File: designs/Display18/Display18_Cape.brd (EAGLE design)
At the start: 71.8 x 58.4 mm, 28 parts, among them T1 3904, X5 SPI-LCD-(1.8IN)

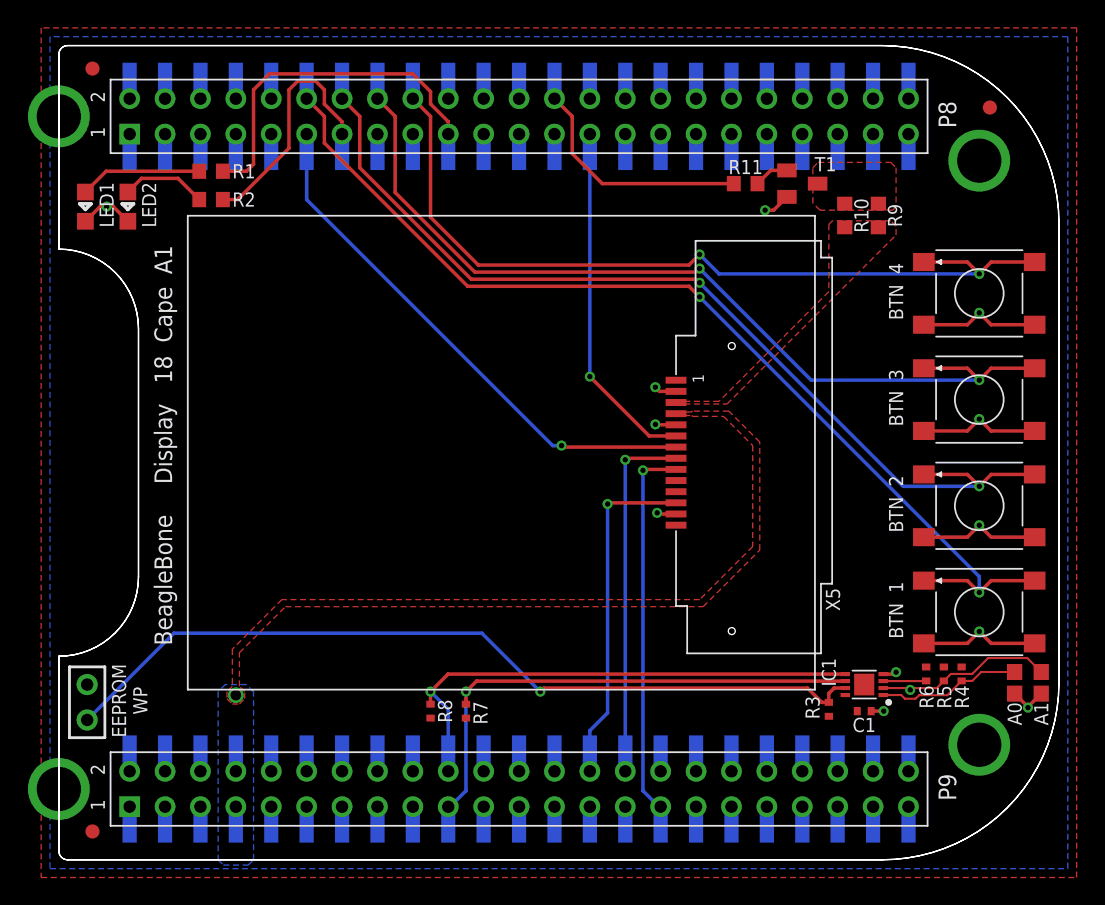
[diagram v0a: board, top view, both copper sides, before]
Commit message: Added the revised EAGLE schematics. Also removed two files that were probably not intended to be added as they are lock files in EAGLE.
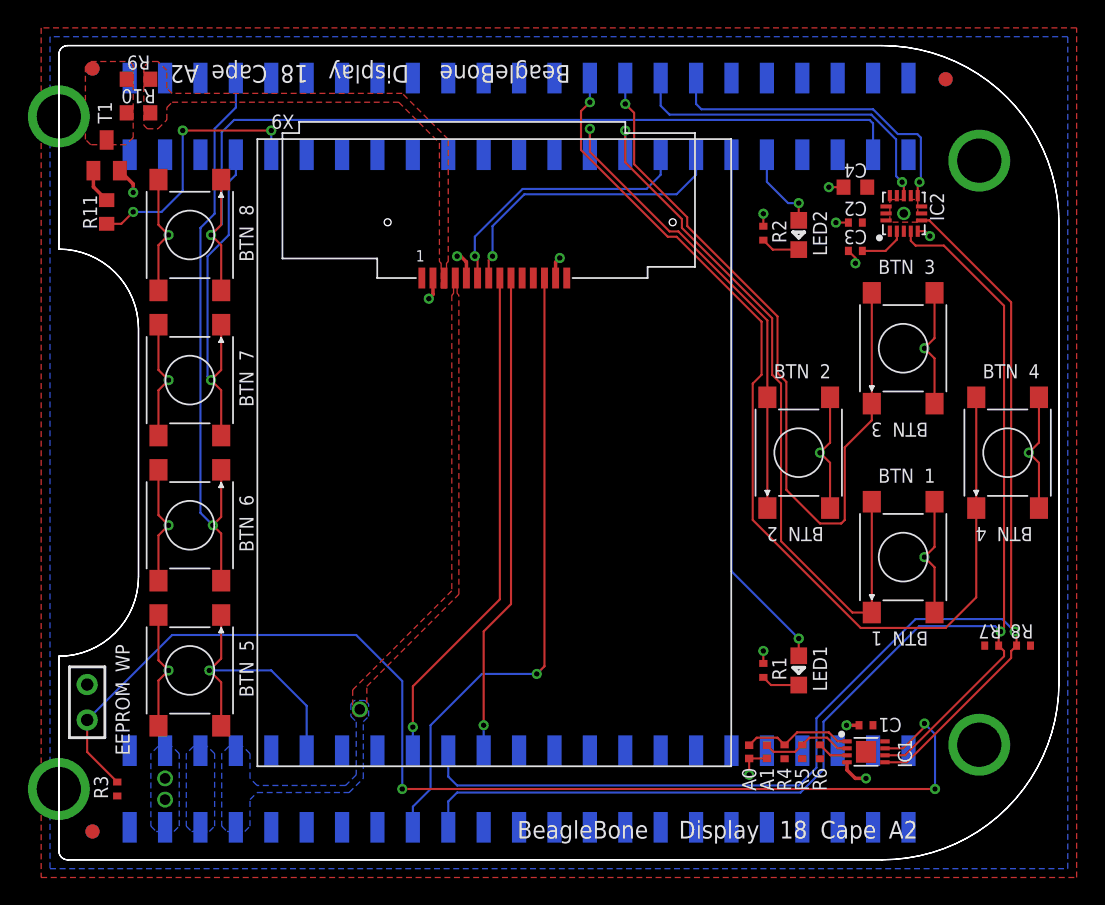
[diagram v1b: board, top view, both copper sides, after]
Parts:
- removed BB.CAPE1: BEAGLEBONE.CAPE.BOTTOM-ONLY-PADS.W/TH, GHI-Solutions:BEAGLEBONE.CAPE.BOTTOM-ONLY-PADS.W/TH
- added BB.CAPE2: BEAGLEBONE.CAPE.BOTTOM-ONLY-PADS, GHI-Solutions:BEAGLEBONE.CAPE.BOTTOM-ONLY-PADS
- added C2, C3: .1uF, GHI-BasicComponents:0402
- added C4: 4.7uF, GHI-BasicComponents:0603
- added FUD4, FUD5, FUD6: FIDUCIAL, GHI:FIDUCIAL_40MIL
- added IC2: (no value), GHI-IC:QFN-16-(MMA8453Q)
- added X6, X7, X8: (no value), GHI2:6MM_TACTILE-SWITCH
- added X9: SPI-LCD-(1.8IN), GHI-Connectors:LCD-(1.8IN)
- C1: value (none) -> .1uF
- R1, R2: device GHI-BasicComponents:0603 -> GHI-BasicComponents:0402
- SJ1, SJ2: device GHI-Miscellaneous:SOLDER.JOINT(0603) -> GHI-Miscellaneous:SOLDER.JOINT(0402)
- X5: value SPI-LCD-(1.8IN) -> (none); device GHI-Connectors:LCD-(1.8IN) -> GHI2:6MM_TACTILE-SWITCH
- moved LED1 61.0 mm to (53.1, 13.6)
- moved R9 54.0 mm to (5.71, 56.0), turned to 180 degrees
- moved R1 53.4 mm to (50.5, 13.6), turned to 270 degrees
- moved R3 51.4 mm to (4.19, 5.08)
- moved R10 51.2 mm to (5.71, 53.6), turned to 180 degrees
- moved T1 50.0 mm to (3.43, 50.5), turned to 0 degrees
- moved LED2 48.2 mm to (53.1, 44.8)
- moved R11 45.9 mm to (3.43, 46.5), turned to 270 degrees
- moved R8 42.8 mm to (69.2, 15.4), turned to 0 degrees
- moved R2 39.7 mm to (50.5, 45.0), turned to 270 degrees
- moved R7 38.0 mm to (66.9, 15.4), turned to 180 degrees
- moved X5 27.3 mm to (9.40, 13.6), turned to 270 degrees
- moved SJ2 20.3 mm to (50.8, 7.75)
- moved SJ1 19.7 mm to (49.5, 7.75)
- moved R4 13.9 mm to (52.1, 7.75), turned to 90 degrees
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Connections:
- removed net BTN1: BB.CAPE1.B8.12, BB.CAPE1.P8.12, X1.1, X1.2
- removed net BTN2: BB.CAPE1.B8.14, BB.CAPE1.P8.14, X2.1, X2.2
- removed net BTN3: BB.CAPE1.B8.16, BB.CAPE1.P8.16, X3.1, X3.2
- removed net BTN4: BB.CAPE1.B8.18, BB.CAPE1.P8.18, X4.1, X4.2
- removed net LCD.BACKLIGHT: BB.CAPE1.B8.26, BB.CAPE1.P8.26, R11.2
- removed net LCD.DC(GPIO45): BB.CAPE1.B8.11, BB.CAPE1.P8.11, X5.7
- removed net LCD.RESET(GPIO86): BB.CAPE1.B8.27, BB.CAPE1.P8.27, X5.6
- removed net LCD.SPI1.CS: BB.CAPE1.B9.28, BB.CAPE1.P9.28, X5.12
- removed net LCD.SPI1.MOSI: BB.CAPE1.B9.30, BB.CAPE1.P9.30, X5.8
- removed net LCD.SPI1.SCK: BB.CAPE1.B9.31, BB.CAPE1.P9.31, X5.9
- removed net LED1: BB.CAPE1.B8.19, BB.CAPE1.P8.19, R1.2
- removed net LED2: BB.CAPE1.B8.13, BB.CAPE1.P8.13, R2.2
- removed net N$282: LED1.A, R1.1
- removed net N$284: LED2.A, R2.1
- new net ACC.IRQ1(GPIO11): BB.CAPE2.B8.32, IC2.11
- new net ACC.IRQ2(GPIO81): BB.CAPE2.B8.34, IC2.9
- new net BTN.1(GPIO87): BB.CAPE2.B8.29, X1.1, X1.2
- new net BTN.2(GPIO86): BB.CAPE2.B8.27, X2.1, X2.2
- new net BTN.3(GPIO89): BB.CAPE2.B8.30, X3.1, X3.2
- new net BTN.4(GPIO88): BB.CAPE2.B8.28, X4.1, X4.2
- new net BTN.5(GPIO60): BB.CAPE2.B9.12, X5.1, X5.2
- new net BTN.6(GPIO67): BB.CAPE2.B8.8, X6.1, X6.2
- new net BTN.7(GPIO66): BB.CAPE2.B8.7, X7.1, X7.2
- new net BTN.8(GPIO72): BB.CAPE2.B8.43, X8.1, X8.2
- new net LCD.BACKLIGHT(TIMER5): BB.CAPE2.B8.9, R11.2
- new net LCD.DC(GPIO9): BB.CAPE2.B8.33, X9.7
- new net LCD.RESET(GPIO10): BB.CAPE2.B8.31, X9.6
- new net LCD.SPI0.CLK: BB.CAPE2.B9.22, X9.9
- new net LCD.SPI0.CS: BB.CAPE2.B9.17, X9.12
- new net LCD.SPI0.MOSI: BB.CAPE2.B9.18, X9.8
- new net LED1(GPIO8): BB.CAPE2.B8.35, LED1.A
- new net LED2(GPIO78): BB.CAPE2.B8.37, LED2.A
- new net N$3: LED2.K, R2.2
- new net N$4: LED1.K, R1.2
- new net N$6: C3.1, IC2.2
- new net VDD_5V: BB.CAPE2.B9.5, BB.CAPE2.B9.6
- net +5V: now also BB.CAPE2.B9.7, BB.CAPE2.B9.8, X9.4; no longer BB.CAPE1.B9.7, BB.CAPE1.B9.8, BB.CAPE1.P9.7, BB.CAPE1.P9.8, X5.4
- net GND: now also BB.CAPE2.B8.1, BB.CAPE2.B8.2, BB.CAPE2.B9.1, BB.CAPE2.B9.2, BB.CAPE2.B9.43, BB.CAPE2.B9.44, BB.CAPE2.B9.45, BB.CAPE2.B9.46, C2.2, C3.2, C4.2, IC2.10, IC2.12, IC2.5, IC2.7, R1.1, R2.1, X5.3, X5.4, X6.3, X6.4, X7.3, X7.4, X8.3, X8.4, X9.13, X9.2, X9.5; no longer BB.CAPE1.B8.1, BB.CAPE1.B8.2, BB.CAPE1.B9.1, BB.CAPE1.B9.2, BB.CAPE1.B9.43, BB.CAPE1.B9.44, BB.CAPE1.B9.45, BB.CAPE1.B9.46, BB.CAPE1.P8.1, BB.CAPE1.P8.2, BB.CAPE1.P9.1, BB.CAPE1.P9.2, BB.CAPE1.P9.43, BB.CAPE1.P9.44, BB.CAPE1.P9.45, BB.CAPE1.P9.46, LED1.K, LED2.K, X5.13, X5.2, X5.5
- net LED.K: now also X9.3; no longer X5.3
- net SCL: now also BB.CAPE2.B9.19, IC2.4; no longer BB.CAPE1.B9.19, BB.CAPE1.P9.19
- net SDA: now also BB.CAPE2.B9.20, IC2.6; no longer BB.CAPE1.B9.20, BB.CAPE1.P9.20
- net VCC: now also BB.CAPE2.B9.3, BB.CAPE2.B9.4, C2.1, C4.1, IC1.8, IC2.1, IC2.14, X9.10, X9.11; no longer BB.CAPE1.B9.3, BB.CAPE1.B9.4, BB.CAPE1.P9.3, BB.CAPE1.P9.4, X5.10, X5.11
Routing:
- net BTN1: track 74.9 -> 0.00 mm, vias 2 -> 0
- net BTN.4(GPIO88): track 0.00 -> 72.5 mm, vias 0 -> 1
- net BTN2: track 69.5 -> 0.00 mm, vias 2 -> 0
- net BTN.8(GPIO72): track 0.00 -> 65.7 mm, vias 0 -> 1
- net BTN3: track 65.1 -> 0.00 mm, vias 2 -> 0
- net BTN4: track 60.9 -> 0.00 mm, vias 2 -> 0
- net SDA: track 37.4 -> 97.0 mm
- net BTN.3(GPIO89): track 0.00 -> 56.7 mm, vias 0 -> 1
- net SCL: track 40.2 -> 95.1 mm
- net BTN.1(GPIO87): track 0.00 -> 52.4 mm, vias 0 -> 1
- net LCD.SPI0.CS: track 0.00 -> 45.6 mm, vias 0 -> 1
- net BTN.6(GPIO67): track 0.00 -> 42.0 mm, vias 0 -> 1
- net LCD.DC(GPIO45): track 38.6 -> 0.00 mm, vias 1 -> 0
- net LED1(GPIO8): track 0.00 -> 37.9 mm, vias 0 -> 1
- net LCD.SPI0.MOSI: track 0.00 -> 36.5 mm, vias 0 -> 1
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- added copper zone on layer 1, net GND
- added copper zone on layer 16, net VCC
- added copper zone on layer 16, net VDD_5V
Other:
- board text added: "5"
- board text added: "6"
- board text added: "7"
- board text added: "8"
- board text added: "A2"
- board text added: "EEPROM"
- board text added: "WP"
- board text removed: "EEPROM WP"
